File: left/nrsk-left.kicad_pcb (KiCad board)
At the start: 2 copper layers, 167.9 x 120.3 mm, 125 parts, among them J1 PJ-320D, J2 USB-C, J3 OLED 128x32, SW1 Esc, SW10 1, SW11 2, SW12 3, SW13 4, SW14 5, SW15 6, SW16 16, SW17 Tab, SW18 Q, SW19 W, SW2 F1, SW20 E, SW21 R, SW22 T, SW23 23, SW24 Ctrl, SW25 A, SW26 S, SW27 D, SW28 F, SW29 G, SW3 F2, SW30 30, SW31 Shift, SW32 Z, SW33 X, SW34 C, SW35 V, SW36 B, SW37 37, SW38 Ctrl, SW39 Opt, SW4 F3, SW40 Cmd, SW41 Space, SW42 Space, SW43 Space, SW44 44, SW5 F4, SW6 F5, SW7 F6, SW8 8, SW9 `, U1 ATmega32U4-AU, U2 USBLC6-2SC6, U3 AS5600-ASOM, Y1 16MHz

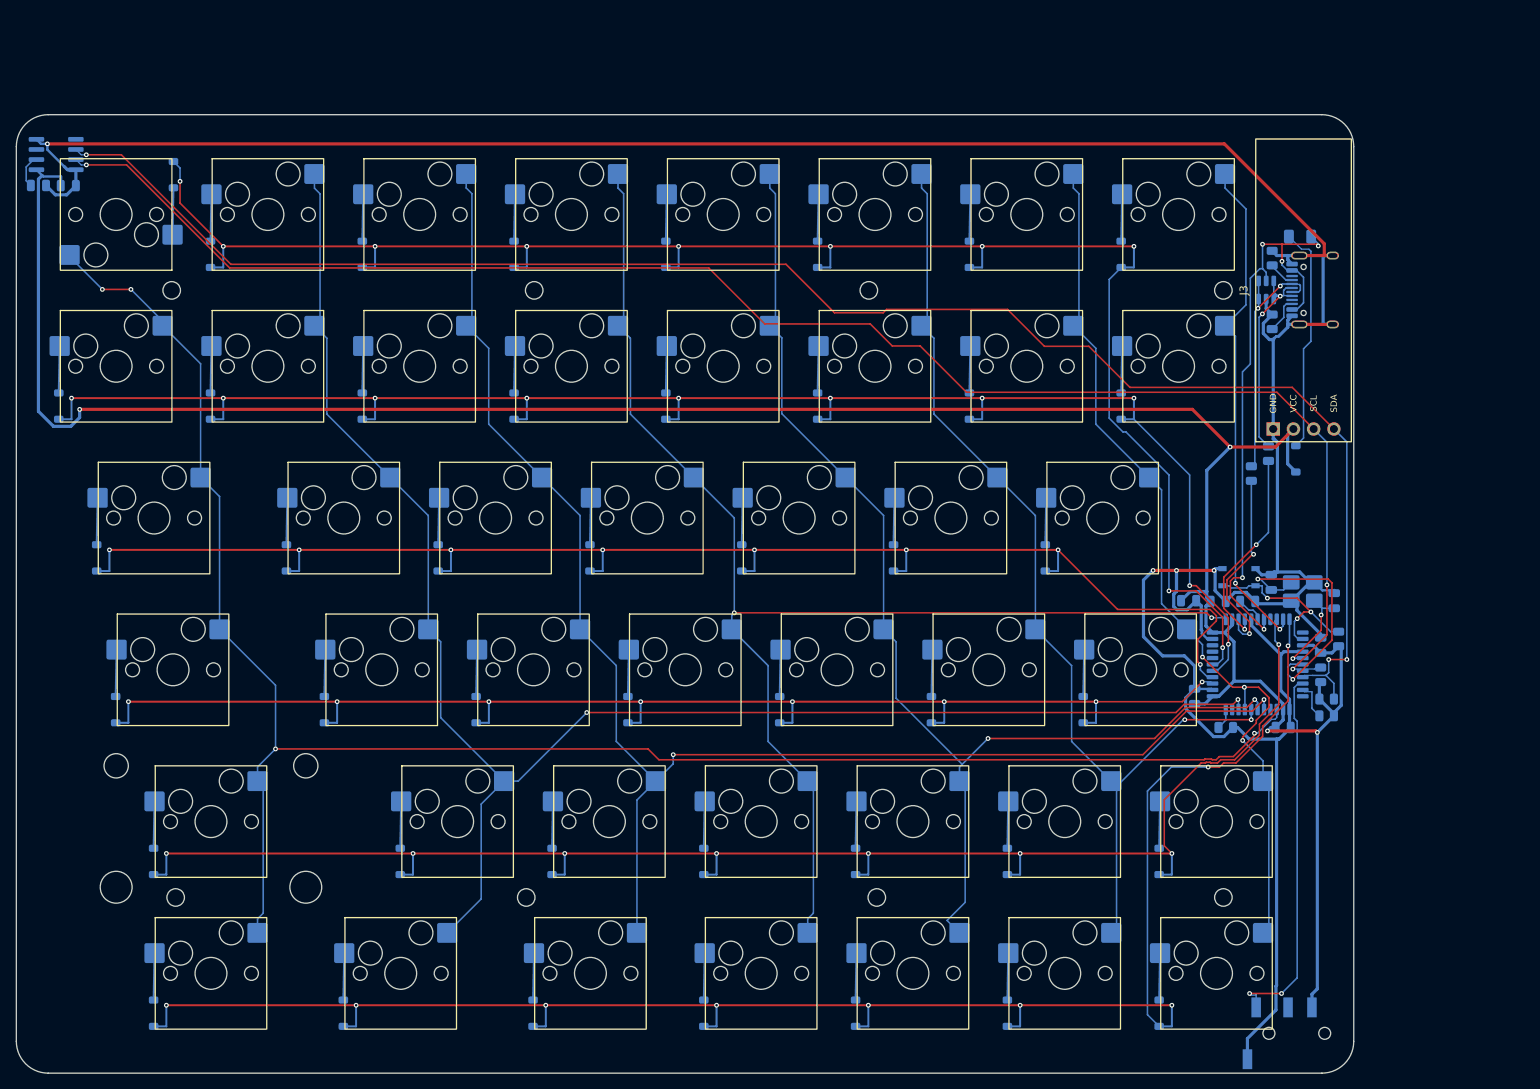
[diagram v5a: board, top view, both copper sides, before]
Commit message: Move to RP2040, rework OLED/connectors/wheel, add all-printed case and assembly guide
- MCU: RP2040 + W25Q128JV + 12 MHz crystal + AP2112K 3.3 V LDO on each half;
  QMK config for RP2040 (UF2, PIO serial, I2C1 on GP2/GP3); routing helped by
  MCU escape stubs, TESTEN-to-pad stub, exposed-pad vias and a fan-out ring
- Boards: top edge +5 mm, inner edges widened; USB-C on the back edge, TRRS
  behind the OLED at the same height on both halves
- OLED: half-mirror acrylic (2 mm) rounded rectangle centred on the display,
  flush with the plate, held by double-sided tape
- Wheel: 32 rim teeth + M3 ball plunger for detents; removable corner cap so
  the printed tray can be assembled; magnet shown in viewer
- Case variants: A (printed tray + clear acrylic plate), B (all printed, plate
  with stiffening web), acrylic stack; slim-head M2 plate screws; tray fillets
- Viewer: shared model-data.js, wheel toggle, rotate below; new interactive
  assembly guide (case/preview/assembly.html, also on Pages)
- BOM: RP2040 parts, plunger, slim-head screws, acrylic finishes, all with
  verified sources; README and renders updated

Co-Authored-By: Claude Opus 5.5 <noreply@anthropic.com>
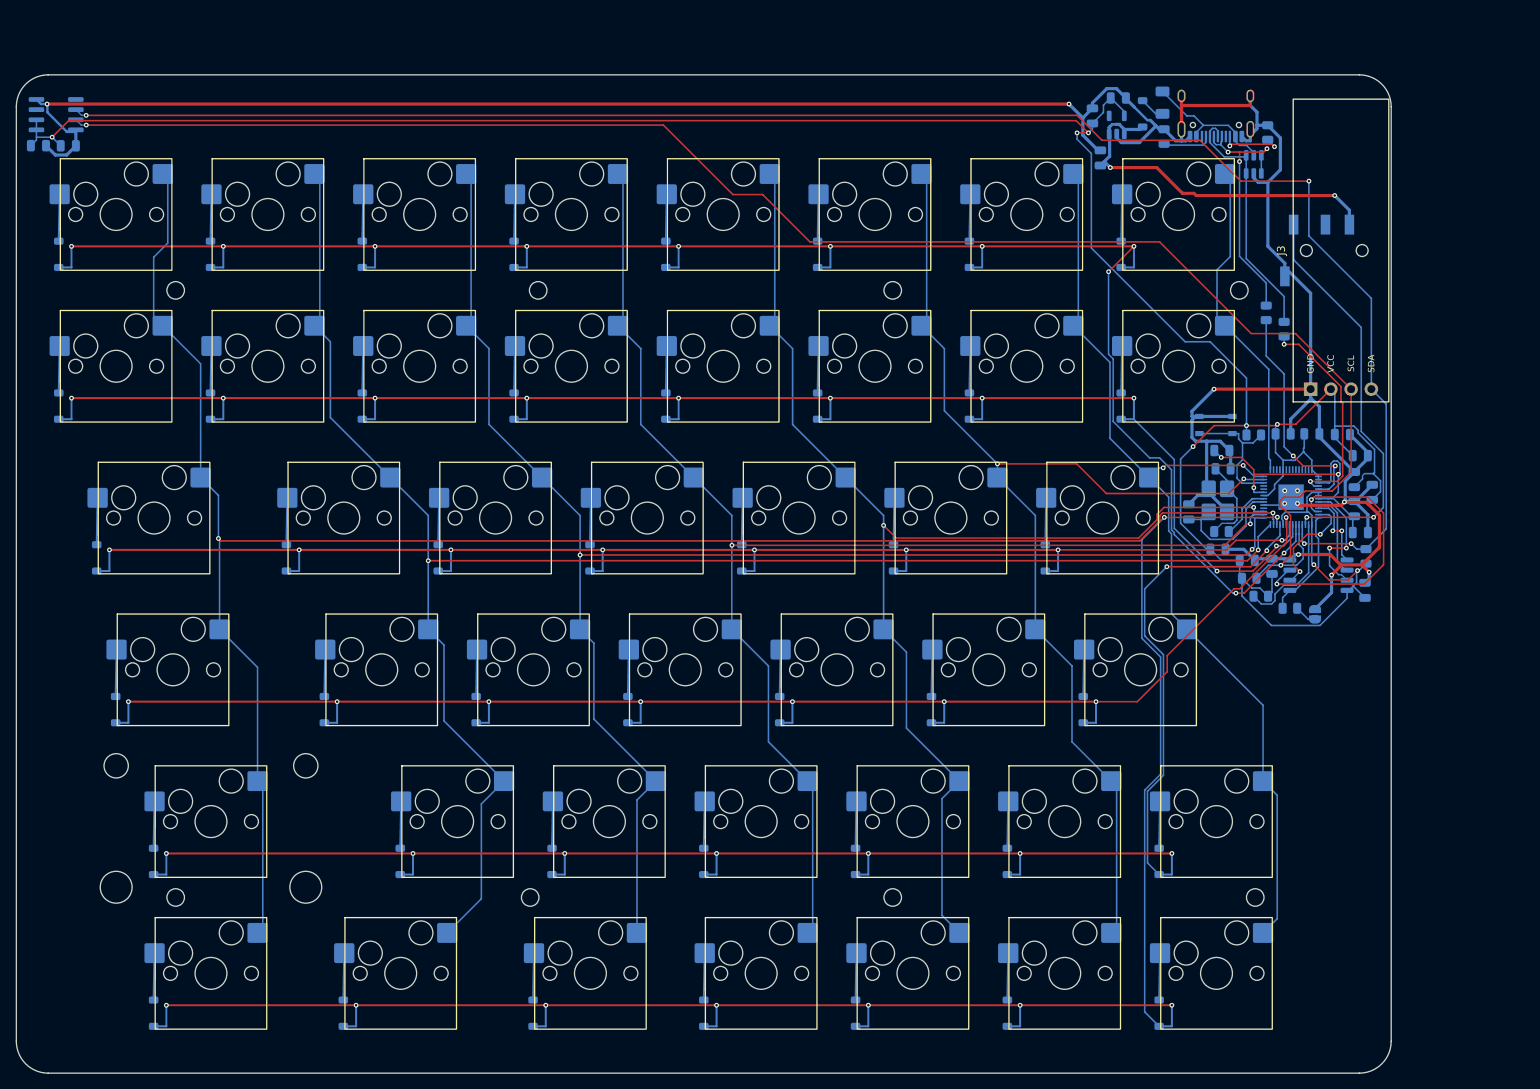
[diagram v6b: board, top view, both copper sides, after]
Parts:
- added C11: 0.1uF, Capacitor_SMD:C_0805_2012Metric, B.Cu at (177.8, 81.5)
- added C12: 0.1uF, Capacitor_SMD:C_0805_2012Metric, B.Cu at (186.0, 67.1)
- added C13: 0.1uF, Capacitor_SMD:C_0805_2012Metric, B.Cu at (189.6, 67.1)
- added C14: 0.1uF, Capacitor_SMD:C_0805_2012Metric, B.Cu at (195.7, 69.8)
- added C15: 0.1uF, Capacitor_SMD:C_0805_2012Metric, B.Cu at (197.2, 74.4)
- added C16: 1uF, Capacitor_SMD:C_0805_2012Metric, B.Cu at (163.1, 32.4)
- added C17: 1uF, Capacitor_SMD:C_0805_2012Metric, B.Cu at (165.3, 24.9)
- added C18: 0.1uF, Capacitor_SMD:C_0805_2012Metric, B.Cu at (193.4, 67.2)
- added C19: 10uF, Capacitor_SMD:C_0805_2012Metric, B.Cu at (162.1, 27.2)
- added C20: 0.1uF, Capacitor_SMD:C_0805_2012Metric, B.Cu at (196.3, 86.7)
- added JP1: BOOTSEL, Jumper:SolderJumper-2_P1.3mm_Open_RoundedPad1.0x1.5mm, B.Cu at (190.0, 89.7)
- added R10: 1k, Resistor_SMD:R_0805_2012Metric, B.Cu at (178.3, 79.3)
- added U4: AP2112K-3.3, Package_TO_SOT_SMD:SOT-23-5, B.Cu at (165.1, 28.3)
- added U5: W25Q128JVS, Package_SO:SOIC-8_5.3x5.3mm_P1.27mm, B.Cu at (190.4, 84.8)
- C1, C2: value 22pF -> 15pF
- C4: value 0.1uF -> 1uF
- C8: value 10uF -> 0.1uF
- R2, R3: value 22 -> 27
- R7: value 10k -> 1k
- U1: value ATmega32U4-AU -> RP2040; footprint Package_QFP:TQFP-44_10x10mm_P0.8mm -> Package_DFN_QFN:QFN-56-1EP_7x7mm_P0.4mm_EP3.2x3.2mm
- Y1: value 16MHz -> 12MHz
- moved J1 98.4 mm to (191.1, 44.0)
- moved D99 47.4 mm to (168.4, 26.9)
- moved R6 27.7 mm to (182.3, 67.2), turned to 0 degrees
- moved C5 27.4 mm to (178.3, 69.2), turned to 0 degrees
- moved J2 27.0 mm to (177.6, 25.7), turned to 0 degrees
- moved C6 26.3 mm to (195.7, 79.5)
- moved F1 24.1 mm to (170.9, 25.5), turned to 90 degrees
- moved R5 23.8 mm to (184.1, 29.2)
- moved C2 21.6 mm to (178.5, 71.5), turned to 0 degrees
- moved U1 21.4 mm to (187.0, 75.0), turned to 90 degrees
- moved C4 20.7 mm to (194.9, 76.5), turned to 90 degrees
- moved R4 20.4 mm to (171.1, 29.7)
- moved C3 20.3 mm to (194.9, 72.8), turned to 90 degrees
- moved RSW1 19.3 mm to (177.6, 66.0)
- moved R3 18.6 mm to (186.1, 53.9)
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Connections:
- C1 pad 1: /XTAL1 -> /XIN
- C10 pad 1: VCC -> /3V3
- C2 pad 1: /XTAL2 -> /XTAL
- C3 pad 1: /UCAP -> /3V3
- C4 pad 1: VCC -> /1V1
- C5 pad 1: VCC -> /1V1
- C6 pad 1: VCC -> /1V1
- C7 pad 1: VCC -> /3V3
- C8 pad 1: VCC -> /3V3
- C9 pad 1: /VDD3V3 -> /3V3
- J3 pad 2: VCC -> /3V3
- R1 pad 2: VCC -> /3V3
- R6 pad 1: VCC -> /3V3
- R6 pad 2: /RST -> /RUN
- R7 pad 1: /HWB -> /QSPI_SS
- R7 pad 2: GND -> /BOOT
- R8 pad 1: VCC -> /3V3
- R9 pad 1: VCC -> /3V3
- RSW1 pad 1: /RST -> /RUN
- U1 pad 1: /COL3 -> /3V3
- U1 pad 10: /COL7 -> /3V3
- U1 pad 11: /ROW5 -> /ROW4
- U1 pad 12: unconnected-(U1-PB7-Pad12) -> /ROW5
- U1 pad 13: /RST -> /COL0
- U1 pad 14: VCC -> /COL1
- U1 pad 15: GND -> /COL2
- U1 pad 16: /XTAL2 -> /COL3
- U1 pad 17: /XTAL1 -> /COL4
- U1 pad 18: /SCL -> unconnected-(U1-GPIO15-Pad18)
- U1 pad 19: /SDA -> GND
- U1 pad 2: VCC -> /HAND
- U1 pad 20: /DATA -> /XIN
- U1 pad 21: /HAND -> /XOUT
- U1 pad 22: unconnected-(U1-PD5-Pad22) -> /3V3
- U1 pad 23: GND -> /1V1
- U1 pad 24: VCC -> unconnected-(U1-SWCLK-Pad24)
- U1 pad 25: /COL0 -> unconnected-(U1-SWDIO-Pad25)
- U1 pad 26: unconnected-(U1-PD6-Pad26) -> /RUN
- U1 pad 27: /COL2 -> /COL5
- U1 pad 28: /COL4 -> /COL6
- U1 pad 29: /COL5 -> /COL7
- U1 pad 3: /D- -> /DATA
- U1 pad 30: /COL6 -> unconnected-(U1-GPIO19-Pad30)
- U1 pad 31: /COL1 -> unconnected-(U1-GPIO20-Pad31)
- U1 pad 33: /HWB -> /3V3
- U1 pad 34: VCC -> unconnected-(U1-GPIO22-Pad34)
- U1 pad 35: GND -> unconnected-(U1-GPIO23-Pad35)
- U1 pad 36: /ROW3 -> unconnected-(U1-GPIO24-Pad36)
- U1 pad 37: /ROW2 -> unconnected-(U1-GPIO25-Pad37)
- U1 pad 38: /ROW1 -> unconnected-(U1-GPIO26/ADC0-Pad38)
- U1 pad 39: /ROW0 -> unconnected-(U1-GPIO27/ADC1-Pad39)
- U1 pad 4: /D+ -> /SDA
- U1 pad 42: unconnected-(U1-AREF-Pad42) -> /3V3
- U1 pad 43: GND -> /3V3
- U1 pad 44: VCC -> /3V3
- U1 pad 5: GND -> /SCL
- U1 pad 6: /UCAP -> /ROW0
- U1 pad 7: /VBUS -> /ROW1
- U1 pad 8: unconnected-(U1-PB0-Pad8) -> /ROW2
- U1 pad 9: /ROW4 -> /ROW3
- U3 pad 1: VCC -> /3V3
- U3 pad 2: /VDD3V3 -> /3V3
- Y1 pad 1: /XTAL1 -> /XIN
- Y1 pad 3: /XTAL2 -> /XTAL
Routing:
- net /3V3: track 0.00 -> 341.6 mm, vias 0 -> 8
- net VCC: track 323.6 -> 45.7 mm, vias 4 -> 2
- net /VBUS: track 75.1 -> 17.4 mm, vias 5 -> 0
- net /1V1: track 0.00 -> 38.1 mm, vias 0 -> 3
- net /QSPI_SD2: track 0.00 -> 35.6 mm, vias 0 -> 2
- net /XTAL1: track 32.6 -> 0.00 mm, vias 2 -> 0
- net GND: track 406.3 -> 377.5 mm, vias 4 -> 11
- net /VFUSE: track 28.7 -> 3.18 mm
- net /RST: track 23.2 -> 0.00 mm, vias 3 -> 0
- net /COL7: track 63.6 -> 40.9 mm, vias 2 -> 0
- net /ROW3: track 166.9 -> 188.6 mm
- net /ROW4: track 194.3 -> 215.5 mm, vias 8 -> 9
- net /ROW5: track 219.5 -> 238.7 mm
- net /RUN: track 0.00 -> 17.4 mm
- net /XIN: track 0.00 -> 15.8 mm
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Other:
- board size 167.9 x 120.3 mm -> 172.6 x 125.3 mm

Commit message: Connector tongues: USB-C / TRRS mouths at the case surface, outline-fit openings
- PCB outline grows a 12 mm tongue under each connector into the case wall;
  the connector mouth sits 0.8 mm inside the outer surface (gen/make_pcb.py)
- Case: openings are just the connector outline + 0.2 mm (rounded slot for
  USB-C, round hole for TRRS); printed tray gets removable port caps over
  the tongues, acrylic frames are notched (gen/make_case.py)
- Port-opening study renders (gen/port_variants.py, docs/img/ports-compare.jpg)
- Viewer, assembly guide (port cap step), BOM, README and images updated

Co-Authored-By: Claude Opus 5.5 <noreply@anthropic.com>
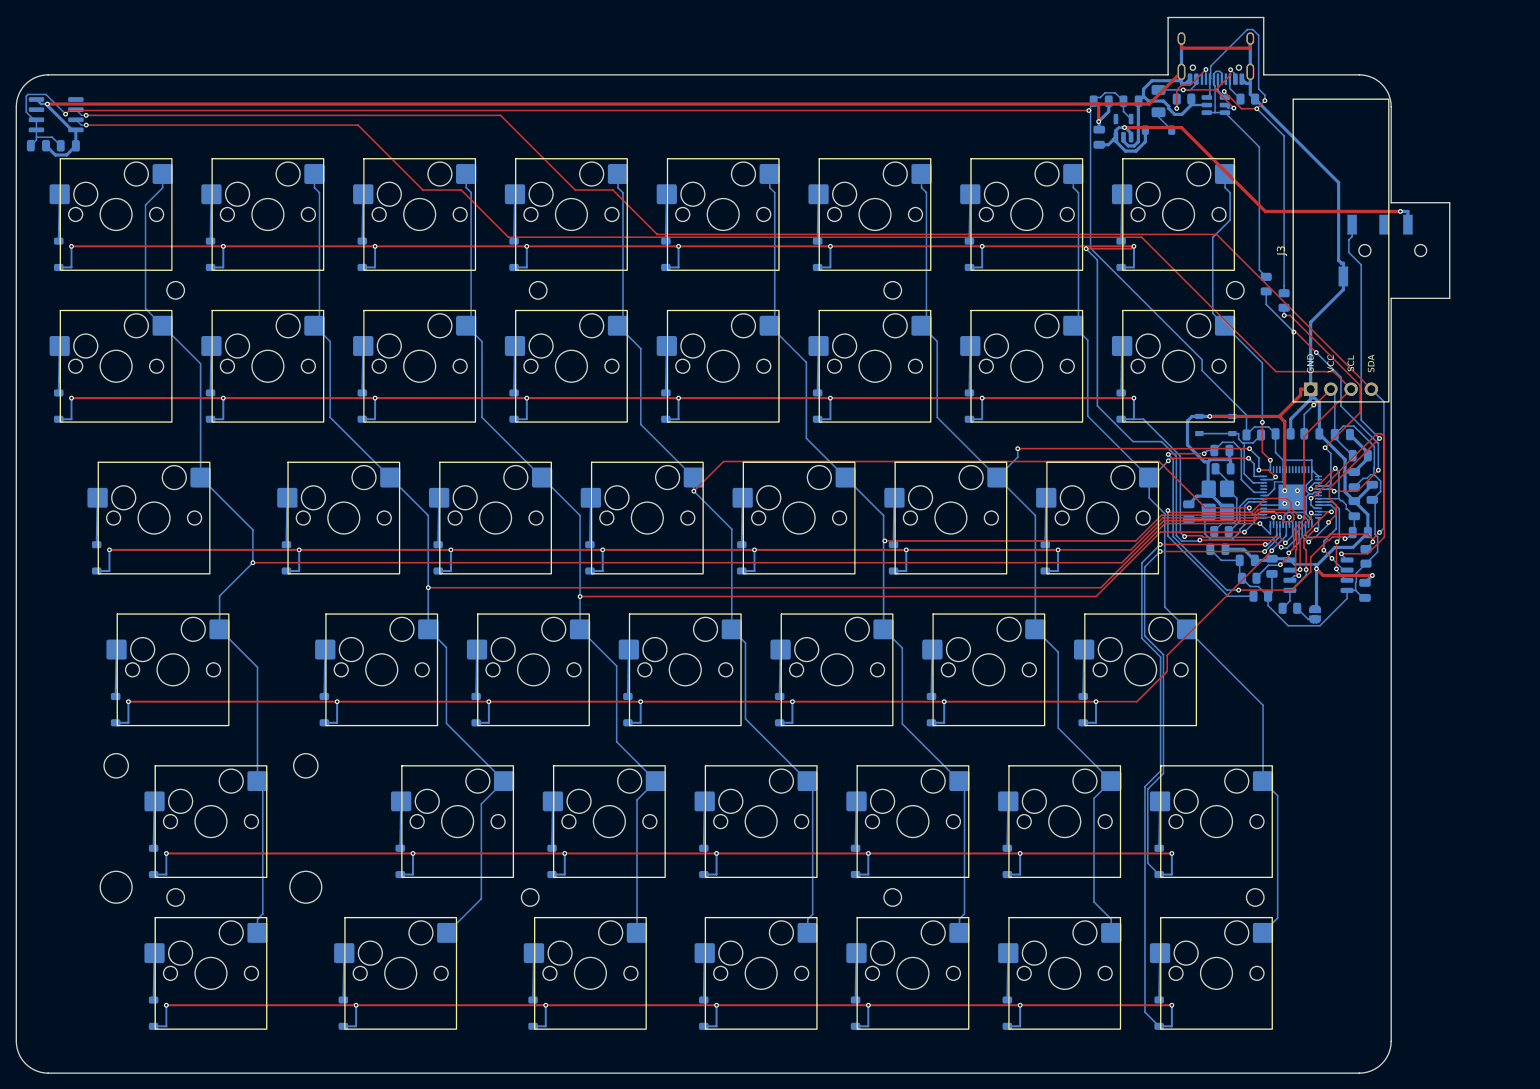
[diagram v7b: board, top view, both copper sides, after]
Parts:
- moved U2 8.84 mm to (177.6, 25.8), turned to 0 degrees
- moved J1 7.34 mm to (198.5, 44.0)
- moved J2 7.20 mm to (177.6, 18.5)
- moved R4 5.32 mm to (173.6, 25.0), turned to 0 degrees
- moved R5 4.89 mm to (181.6, 25.0), turned to 0 degrees
- moved R3 3.60 mm to (186.1, 50.3)
- moved R2 3.60 mm to (183.9, 48.3)
- moved D99 2.86 mm to (170.4, 28.9), turned to 0 degrees
- moved C16 2.60 mm to (162.9, 29.8)
- moved C19 2.15 mm to (163.2, 25.3), turned to 0 degrees
- moved C17 1.65 mm to (166.9, 25.3)
- moved U4 0.94 mm to (166.0, 28.7)
- moved F1 0.54 mm to (170.4, 25.3)
- moved H4 0.50 mm to (180.0, 49.0)
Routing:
- net /1V1: track 38.1 -> 75.0 mm, vias 3 -> 6
- net /QSPI_SD0: track 9.54 -> 34.6 mm
- net /USB_D-: track 31.6 -> 55.3 mm, vias 0 -> 3
- net /3V3: track 341.6 -> 318.2 mm, vias 8 -> 3
- net /QSPI_SD2: track 35.6 -> 12.1 mm
- net /HAND: track 15.5 -> 37.6 mm, vias 0 -> 2
- net GND: track 377.5 -> 390.4 mm, vias 11 -> 9
- net /SDA: track 220.3 -> 210.1 mm
- net VCC: track 45.7 -> 54.3 mm
- net /D+: track 28.8 -> 37.1 mm, vias 2 -> 4
- net /SCL: track 215.6 -> 207.6 mm, vias 2 -> 3
- net /COL3: track 175.0 -> 182.2 mm
- net /COL5: track 142.0 -> 148.5 mm, vias 2 -> 4
- net /COL4: track 158.3 -> 164.5 mm
- net /CC2: track 8.22 -> 3.05 mm, vias 2 -> 0
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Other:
- board size 172.6 x 125.3 mm -> 179.9 x 132.5 mm
